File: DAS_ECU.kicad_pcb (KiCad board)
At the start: 2 copper layers, 156 x 85 mm, 131 parts, among them J1 Raspberry_Pi_2_3, J10 WHEEL_RIGHT, J11 BUZZER, J12 SD, J2 CAN, J3 POWER, J4 SWDEBUG_CONN, J5 BRAKELIGHT, J6 PEDAL_BOX, J7 BRAKE_REAR, J8 STEERING_WHEEL, J9 WHEEL_LEFT, K1 EX12U1S, Q1 2N7002NXAKR, Q2 2N7002NXAKR, Q3 2N7002NXAKR, Q4 2N7002NXAKR, Q5 2N7002NXAKR, SW1 RESET, U1 Tex_DCDC, U10 MCP2562-E-SN, U11 MCP2562-E-SN, U12 STM32F446RETx, U13 M95256-WMN6P, U14 BMI088, U2 LD1117S50TR_SOT223, U3 MAX490E, U4 LM358, U5 MP3V5004DP, U6 LM358, U7 MCP2562-E-SN, U8 UA9637A, U9 UA9637A, Y1 ECS-160-18-33 16Mhz

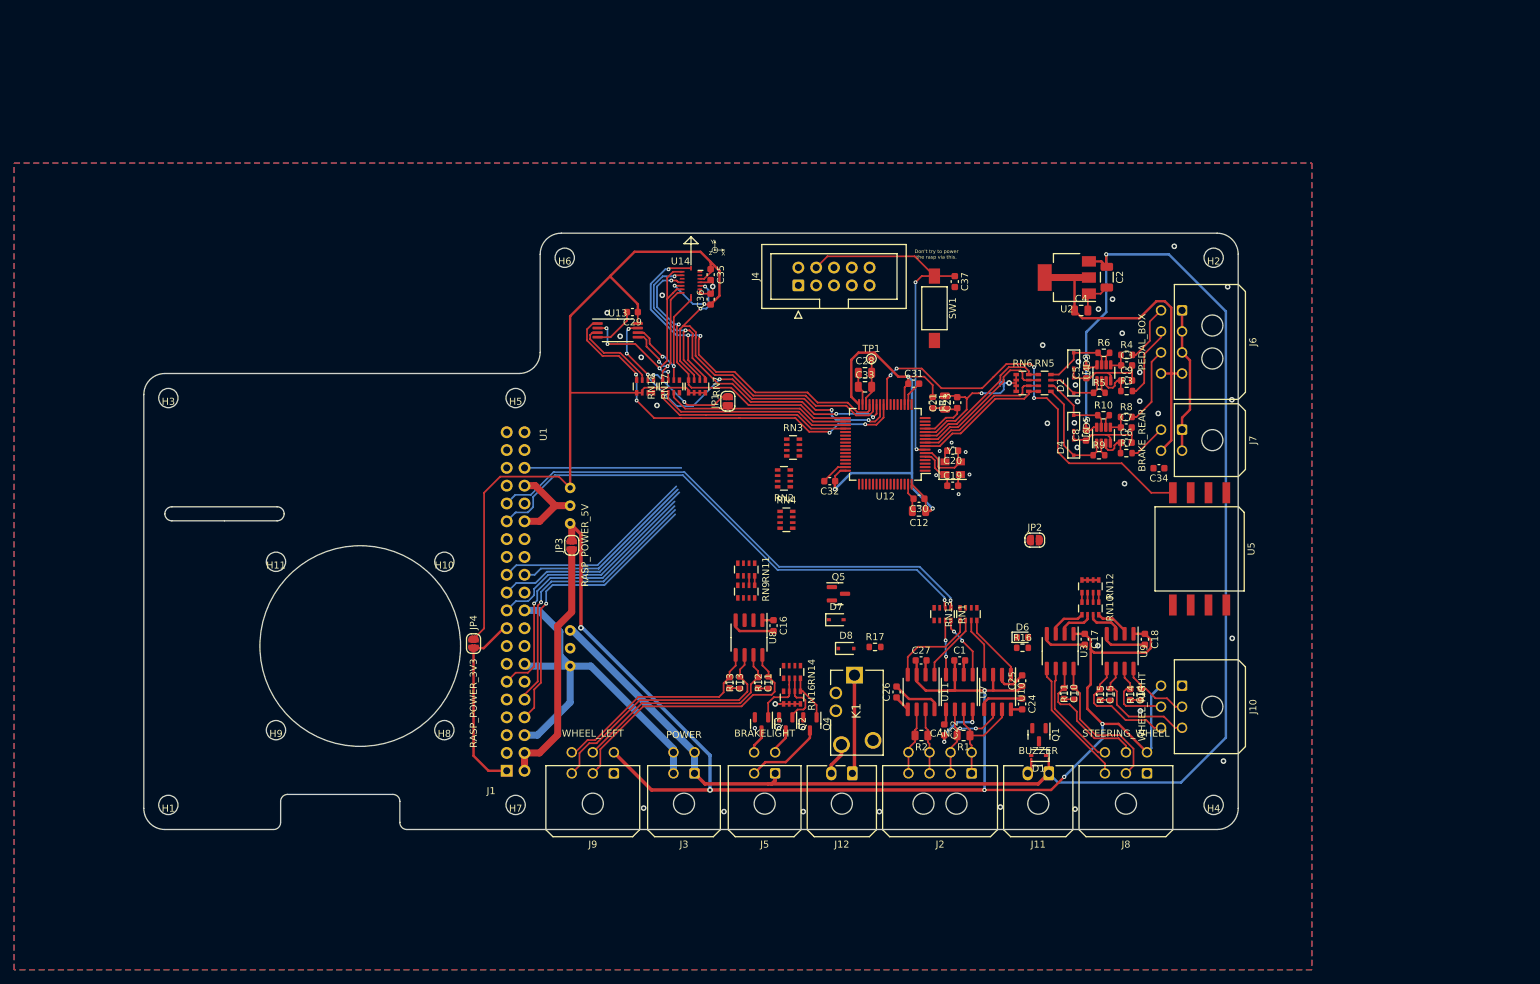
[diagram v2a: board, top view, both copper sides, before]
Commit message: Board finished electrically, passes ERC/DRC
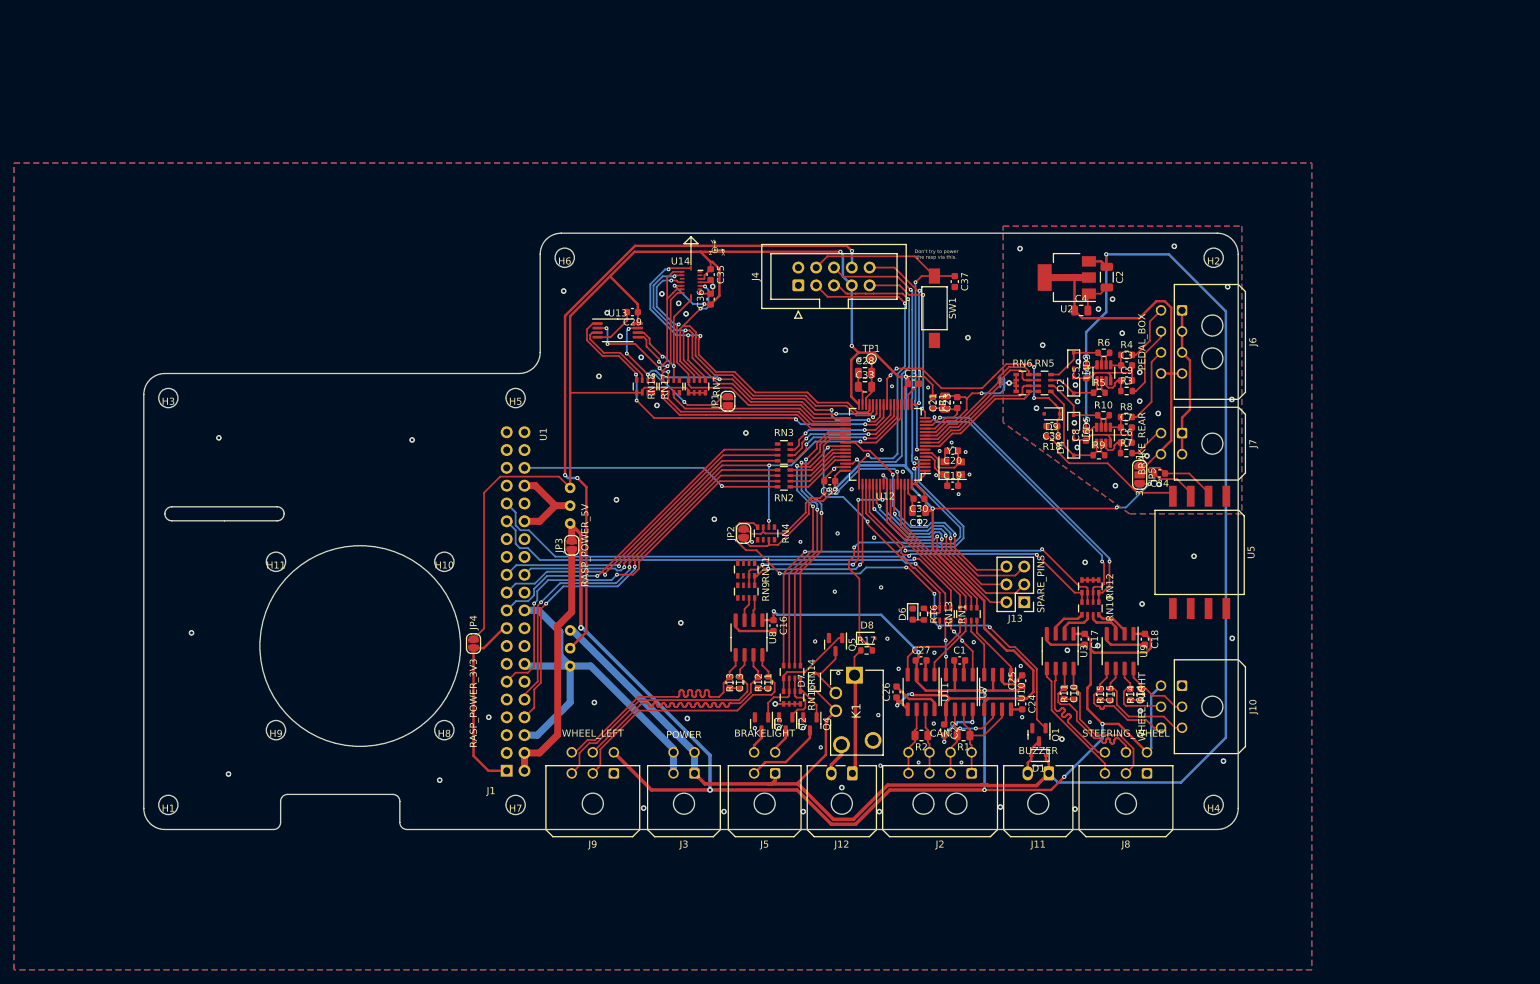
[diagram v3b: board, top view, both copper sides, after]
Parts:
- added C38: 100nF, Capacitor_SMD:C_0603_1608Metric, F.Cu at (214.9, 78.5)
- added D9: DDZ3V3ASF 3.3V, Diode_SMD:D_SOD-323F, F.Cu at (214.9, 76.8)
- added J13: SPARE_PINS, Connector_PinHeader_2.54mm:PinHeader_2x03_P2.54mm_Vertical, F.Cu at (211.0, 103.6)
- added JP5: SolderJumper_3, Jumper:SolderJumper-3_P1.3mm_Open_RoundedPad1.0x1.5mm_NumberLabels, F.Cu at (227.4, 85.5)
- added R18: 100, Resistor_SMD:R_0603_1608Metric, F.Cu at (214.9, 80.0)
- moved JP2 41.5 mm to (171.0, 93.8), turned to 90 degrees
- moved D6 16.0 mm to (195.1, 105.3), turned to 270 degrees
- moved R16 14.8 mm to (196.7, 105.3), turned to 270 degrees
- moved D7 9.24 mm to (181.1, 114.8), turned to 90 degrees
- moved Q5 7.26 mm to (184.1, 109.7), turned to 270 degrees
- moved RN4 3.49 mm to (174.2, 93.8), turned to 270 degrees
- moved D8 3.33 mm to (188.6, 108.8)
- moved RN3 1.48 mm to (176.8, 82.2)
- moved R17 1.30 mm to (188.5, 110.5)
- moved C34 0.76 mm to (230.3, 85.2)
- moved J7 0.50 mm to (233.5, 79.5)
- moved U5 0.50 mm to (236.0, 96.5)
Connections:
- C34 pad 1: +3V3 -> Net-(C34-Pad1)
- RN1 pad 3: Net-(RN1-Pad3) -> /Brain_Rasp/BUZZER
- RN1 pad 6: Net-(RN1-Pad6) -> /Brain_Rasp/BUZZER_1
- RN3 pad 1: /Brain_Rasp/BUZZER_1 -> Net-(RN3-Pad1)
- RN3 pad 2: /Brain_Rasp/RASP_SPI_CLK -> /Brain_Rasp/RASP_SPI_MOSI
- RN3 pad 3: /Brain_Rasp/RASP_SPI_MOSI -> /Brain_Rasp/RASP_SPI_MISO
- RN3 pad 4: /Brain_Rasp/RASP_SPI_MISO -> /Brain_Rasp/RASP_SPI_CLK
- RN3 pad 5: /Brain_Rasp/MCU_SPI_MISO -> /Brain_Rasp/MCU_SPI_CLK
- RN3 pad 6: /Brain_Rasp/MCU_SPI_MOSI -> /Brain_Rasp/MCU_SPI_MISO
- RN3 pad 7: /Brain_Rasp/MCU_SPI_CLK -> /Brain_Rasp/MCU_SPI_MOSI
- RN3 pad 8: /Brain_Rasp/BUZZER -> Net-(RN3-Pad8)
- U12 pad 40: Net-(U12-Pad40) -> /Brain_Rasp/PC9
- U12 pad 53: Net-(U12-Pad53) -> /Brain_Rasp/PC12
- U12 pad 54: Net-(U12-Pad54) -> /Brain_Rasp/PD2
- U12 pad 56: Net-(U12-Pad56) -> /Brain_Rasp/PB4
- U12 pad 59: Net-(U12-Pad59) -> /Brain_Rasp/PB7
- U5 pad 2: +3V3 -> Net-(C34-Pad1)
- U5 pad 4: /Analog_Sensors/PITOT_PD -> Net-(R18-Pad2)
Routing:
- net +3V3: track 210.4 -> 354.2 mm, vias 5 -> 11
- net /5V_PROG: track 0.00 -> 98.1 mm, vias 0 -> 3
- net /Brain_Rasp/BUZZER_1: track 0.00 -> 69.2 mm, vias 0 -> 5
- net /SD_CLOSE: track 0.00 -> 56.5 mm, vias 0 -> 2
- net /Brain_Rasp/MCU_SPI_CS: track 26.9 -> 74.4 mm, vias 0 -> 4
- net /SD_IN_3V3: track 0.00 -> 46.6 mm, vias 0 -> 2
- net /SWCLK: track 0.00 -> 45.0 mm, vias 0 -> 2
- net /SWDIO: track 0.00 -> 43.0 mm, vias 0 -> 2
- net /Brain_Rasp/WR_A: track 1.35 -> 42.2 mm, vias 0 -> 2
- net /Brain_Rasp/WR_B: track 1.35 -> 41.9 mm, vias 0 -> 2
- net /Brain_Rasp/SW_DATA: track 1.35 -> 41.9 mm, vias 0 -> 2
- net /Brain_Rasp/SW_CLK: track 1.35 -> 41.5 mm, vias 0 -> 2
- net /BL_CH3: track 0.00 -> 40.1 mm, vias 0 -> 2
- net /BL_CH2: track 0.00 -> 40.0 mm, vias 0 -> 2
- net /BL_CH1: track 0.00 -> 39.5 mm, vias 0 -> 2
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- added copper zone on B.Cu, net GND1
- added copper zone on F.Cu, net GND1
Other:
- net class SDC added: clearance 0.5, trace_width 0.35, via_dia 0.55, via_drill 0.25

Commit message: Print ready v1.0
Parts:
- added G***: LOGO, Eagle_Logos:scritta_scale500, B.Cu at (174.8, 94.5)
- added G***: LOGO, Eagle_Logos:logo_40mm, B.Cu at (210.4, 79.7)
- added G***: LOGO, Eagle_Logos:logo_12mm3_3000scale, F.Cu at (219.0, 95.1)
- added G***: LOGO, Eagle_Logos:scritta_scale600, F.Cu at (190.4, 100.9)
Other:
- board text added: "20220110 - v1.0"
- board text added: "DAS"
- board text added: "DAS+ECU"
- board text added: "ECU"

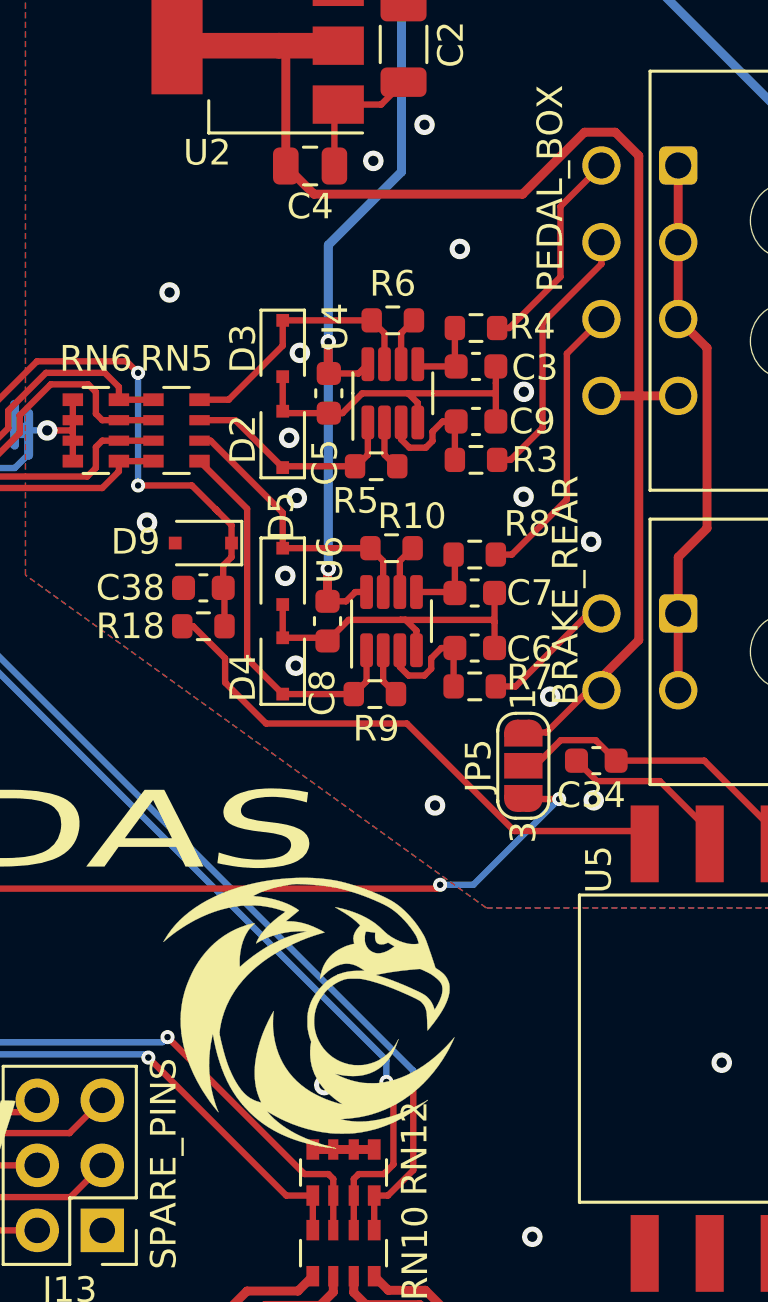
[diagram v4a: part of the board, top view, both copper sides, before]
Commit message: changed to LM358PWR
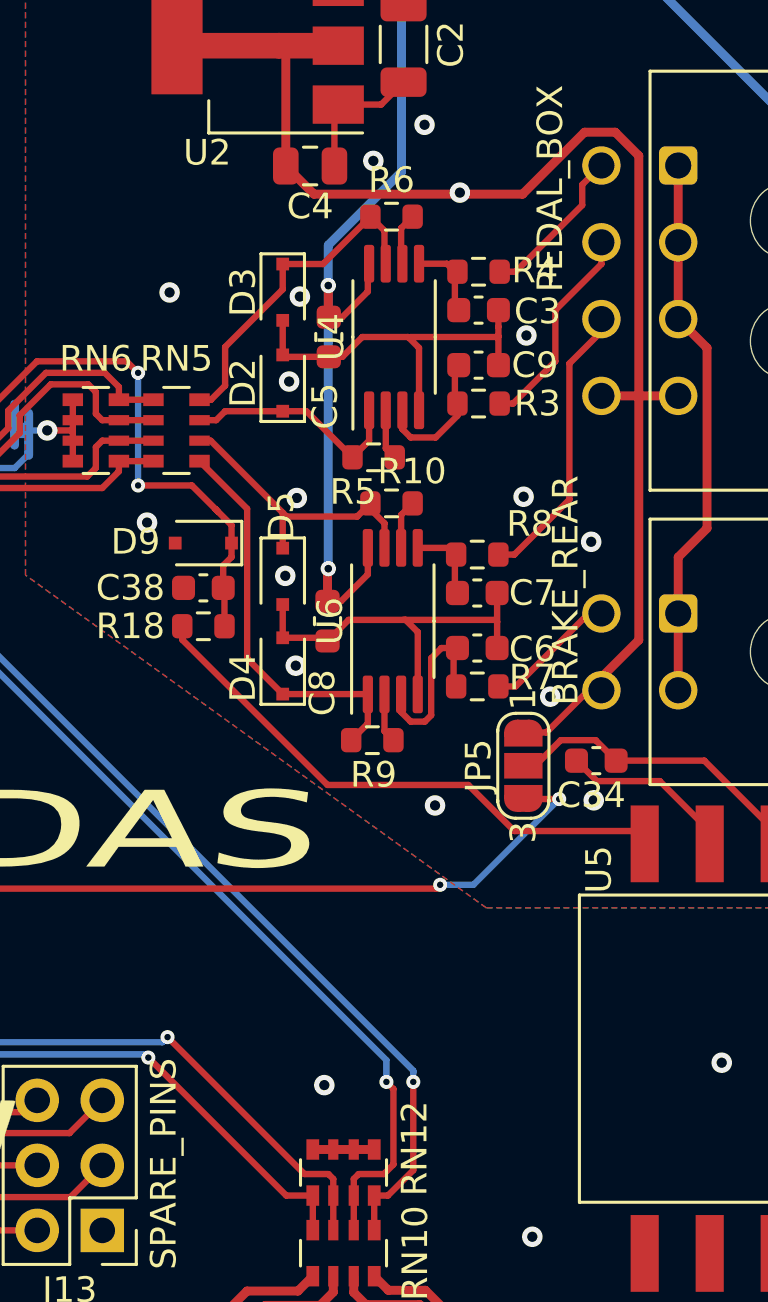
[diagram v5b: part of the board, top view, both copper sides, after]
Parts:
- removed the G*** at (219.0, 95.1)
- U4, U6: value LM358 -> LM358PWR; footprint Package_TO_SOT_SMD:TSOT-23-8 -> Package_SO:TSSOP-8_4.4x3mm_P0.65mm
- moved R6 4.05 mm to (222.3, 64.0)
- moved C9 2.20 mm to (225.7, 69.8)
- moved R3 2.20 mm to (225.7, 71.3)
- moved C3 2.20 mm to (225.7, 67.7)
- moved R4 2.20 mm to (225.7, 66.2)
- moved U4 2.20 mm to (222.4, 68.7)
- moved C5 2.20 mm to (219.8, 68.7)
- moved D2 2.20 mm to (218.1, 70.5)
- moved D3 2.20 mm to (218.1, 67.0)
- moved R9 1.80 mm to (221.6, 84.5)
- moved R10 1.75 mm to (222.3, 75.2)
- moved R5 0.36 mm to (221.6, 73.4)
- moved C6 0.10 mm to (225.7, 80.8)
- moved C7 0.10 mm to (225.7, 78.7)
- moved R7 0.10 mm to (225.7, 82.3)
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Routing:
- net GND1: track 83.5 -> 87.0 mm, vias 22 -> 21
- net +12V: track 250.6 -> 253.4 mm
- net /Analog_Sensors/ACC_1_BUF: track 10.5 -> 13.2 mm
- net /Analog_Sensors/ACC_S2: track 10.5 -> 8.25 mm
- net /Analog_Sensors/ACC_S1: track 8.32 -> 6.16 mm
- net Net-(C6-Pad1): track 5.15 -> 6.96 mm
- net /Analog_Sensors/BRAKE_R_BUF: track 15.1 -> 15.8 mm
- net /Analog_Sensors/5V_SENSORS: vias 0 -> 1

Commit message: changes
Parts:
- added JP6: SolderJumper_2_Open, Jumper:SolderJumper-2_P1.3mm_Open_RoundedPad1.0x1.5mm, F.Cu at (186.2, 63.5)
- added JP7: SolderJumper_2_Open, Jumper:SolderJumper-2_P1.3mm_Open_RoundedPad1.0x1.5mm, F.Cu at (182.8, 63.5)
- added REF**: MountingHole_3.2mm_M3_ISO14580, MountingHole:MountingHole_3.2mm_M3_ISO14580, F.Cu at (131.1, 56.9)
- added REF**: MountingHole_3.2mm_M3_DIN965, MountingHole:MountingHole_3.2mm_M3_DIN965, F.Cu at (96.0, 74.6)
- added REF**: MountingHole_3.2mm_M3, MountingHole:MountingHole_3.2mm_M3, F.Cu at (136.8, 54.5)
- D9: value DDZ3V3ASF 3.3V -> DDZ3V3ASF 3V3
- U1: value Tex_DCDC -> Tex_DCDC_v2; footprint Eagle_Main:Tex_DCDC_horizontal -> Eagle_Main:Tex_DCDC_v2_horizontal
- moved JP3 29.1 mm to (143.0, 124.4)
- moved U1 5.83 mm to (146.9, 94.2), turned to 0 degrees
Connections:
- J4 pad 7: +3V3 -> Net-(J4-Pad7)
- J4 pad 8: /5V_PROG -> Net-(J4-Pad8)
- U1 pad 3: +5V -> GND
- U1 pad 4: +12V -> +5V
- U1 pad 5: /5V_PROG -> +5V
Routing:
- net /5V_PROG: track 98.0 -> 0.00 mm, vias 3 -> 0
- net +5V: track 244.8 -> 331.8 mm, vias 8 -> 9
- net Net-(J1-Pad2): track 35.5 -> 5.79 mm
- net /Brain_Rasp/RASP_RX: track 57.0 -> 72.8 mm, vias 2 -> 0
- net /Brain_Rasp/RASP_TX: track 58.7 -> 73.9 mm, vias 2 -> 0
- net /Brain_Rasp/RASP_SPI_MOSI: track 48.6 -> 58.8 mm, vias 1 -> 0
- net Net-(J4-Pad8): track 0.00 -> 8.83 mm, vias 0 -> 1
- net /Brain_Rasp/RASP_SPI_MISO: track 47.2 -> 54.8 mm, vias 1 -> 0
- net /Brain_Rasp/RASP_RTS: track 57.1 -> 62.8 mm, vias 2 -> 0
- net +12V: track 253.4 -> 258.7 mm
- net Net-(J4-Pad7): track 0.00 -> 5.22 mm, vias 0 -> 1
- net +3V3: track 354.2 -> 359.0 mm, vias 11 -> 12
- net /Brain_Rasp/RASP_SPI_CLK: track 45.7 -> 50.3 mm, vias 1 -> 0
- net /Brain_Rasp/MCU_SPI_CS: track 74.4 -> 78.8 mm, vias 4 -> 3
- net GND: track 154.9 -> 152.8 mm, vias 82 -> 84
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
